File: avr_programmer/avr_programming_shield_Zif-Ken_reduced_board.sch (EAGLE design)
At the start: 17 parts

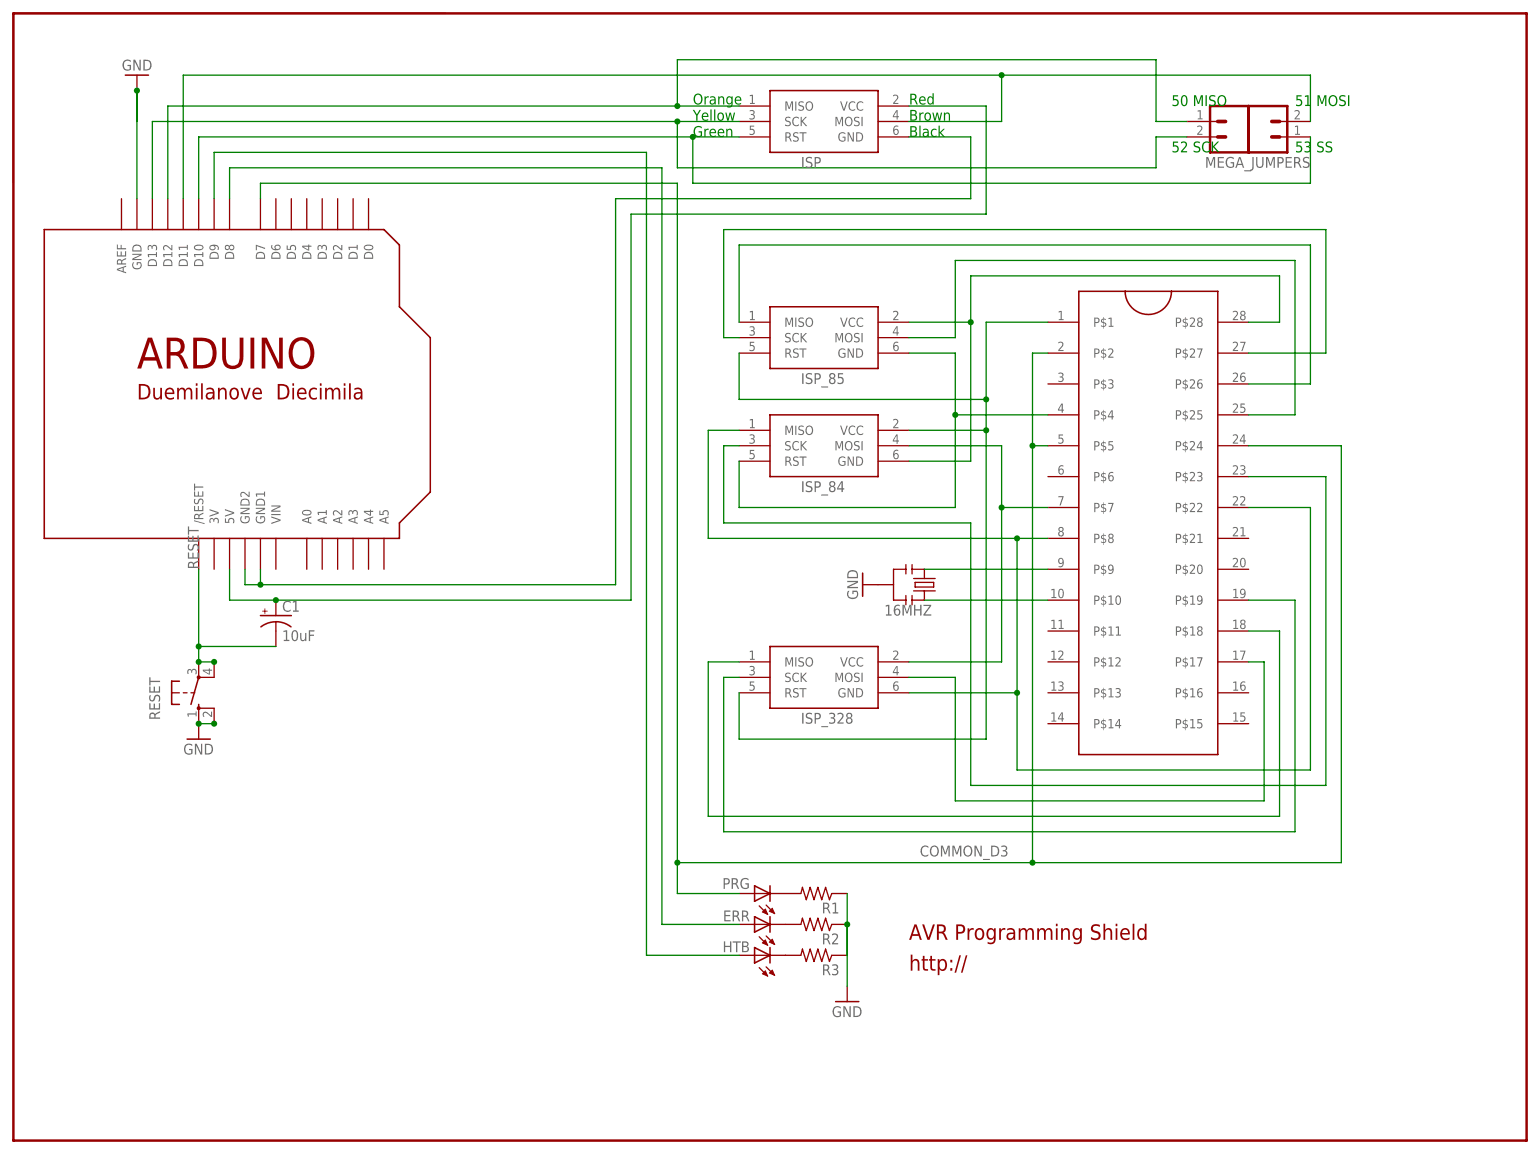
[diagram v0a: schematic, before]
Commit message: updating Zif footprint
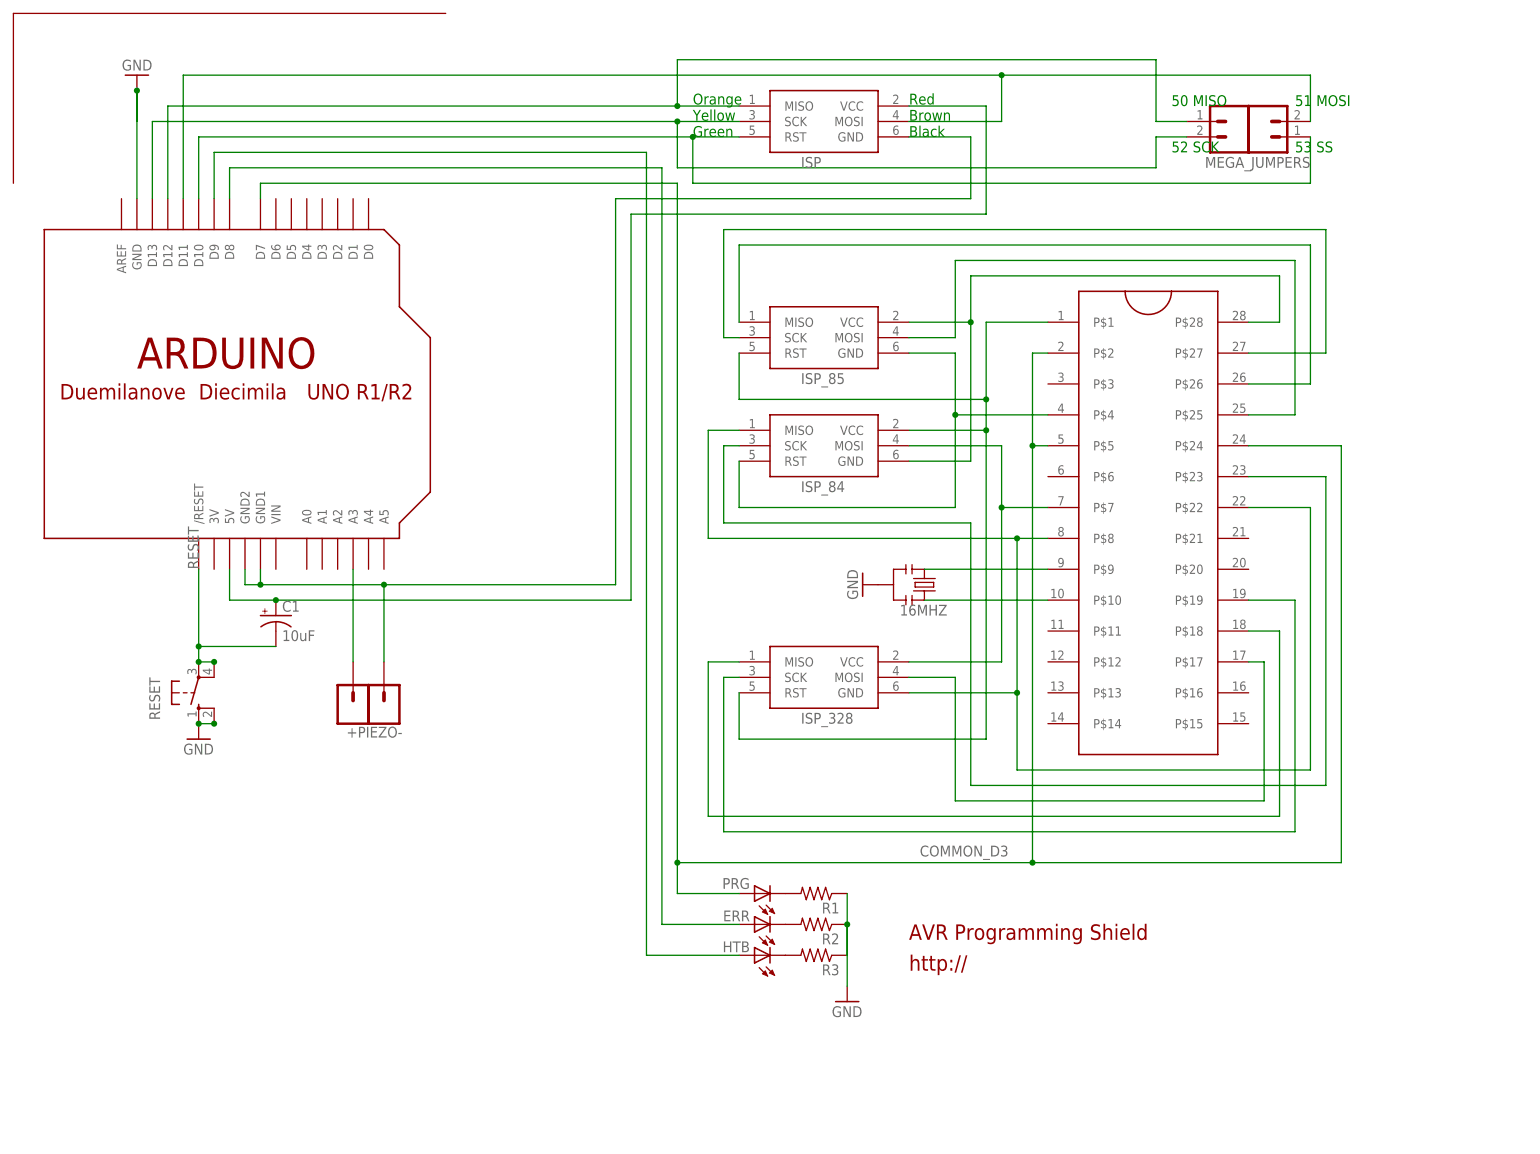
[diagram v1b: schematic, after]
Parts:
- removed U$3: ZIFSOCKET-28-3ZIFFSOCKET-28-3, SparkFun-Connectors_mod:ZIFSOCKET-28-3ZIFFSOCKET-28-3
- added +PIEZO-, JP4: M01PTH, SparkFun-Connectors_mod:M01PTH
- added U$4: ZIFSOCKET-28-3ZIFFSOCKET-28-3, SparkFun_mod:ZIFSOCKET-28-3ZIFFSOCKET-28-3
- 16MHZ: device SparkFun:RESONATORPTH -> SparkFun_mod:RESONATORPTH
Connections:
- new net N$12: JP4.1, U$1.A3
- net COMMON_D3: now also U$4.P$2, U$4.P$24, U$4.P$5; no longer U$3.P$2, U$3.P$24, U$3.P$5
- net GND: now also +PIEZO-.1
- net N$1: now also U$4.P$17; no longer U$3.P$17
- net N$11: now also U$4.P$7; no longer U$3.P$7
- net N$13: now also U$4.P$1; no longer U$3.P$1
- net N$15: now also U$4.P$23; no longer U$3.P$23
- net N$16: now also U$4.P$28; no longer U$3.P$28
- net N$18: now also U$4.P$4; no longer U$3.P$4
- net N$19: now also U$4.P$25; no longer U$3.P$25
- net N$20: now also U$4.P$26; no longer U$3.P$26
- net N$21: now also U$4.P$27; no longer U$3.P$27
- net N$22: now also U$4.P$9; no longer U$3.P$9
- net N$25: now also U$4.P$10; no longer U$3.P$10
- net N$26: now also U$4.P$22, U$4.P$8; no longer U$3.P$22, U$3.P$8
- net N$4: now also U$4.P$18; no longer U$3.P$18
- net N$7: now also U$4.P$19; no longer U$3.P$19
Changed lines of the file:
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@@
 <part name="ISP_85" library="adafruit" deviceset="AVRISP" device="-6"/>
 <part name="C1" library="SparkFun" deviceset="CAP_POL" device="PTH2" value="10uF"/>
-<part name="16MHZ" library="SparkFun" deviceset="RESONATOR" device="PTH"/>
 <part name="GND3" library="supply1" deviceset="GND" device=""/>
 <part name="MEGA_JUMPERS" library="SparkFun" deviceset="M02" device="PTH"/>
 <part name="JP2" library="SparkFun" deviceset="M02" device="PTH"/>
-<part name="U$3" library="SparkFun-Connectors_mod" deviceset="ZIFSOCKET-28-3" device="ZIFFSOCKET-28-3"/>
+<part name="16MHZ" library="SparkFun_mod" deviceset="RESONATOR" device="PTH"/>
+<part name="U$4" library="SparkFun_mod" deviceset="ZIFSOCKET-28-3" device="ZIFFSOCKET-28-3"/>
+<part name="JP4" library="SparkFun-Connectors_mod" deviceset="M01" device="PTH"/>
+<part name="+PIEZO-" library="SparkFun-Connectors_mod" deviceset="M01" device="PTH"/>
 </parts>
 <sheets>
@@
 <instance part="ISP_85" gate="G$1" x="132.08" y="132.08"/>
 <instance part="C1" gate="G$1" x="43.18" y="86.36"/>
-<instance part="16MHZ" gate="G$1" x="149.86" y="91.44" smashed="yes" rot="R270">
-<attribute name="NAME" x="143.256" y="86.36" size="1.778" layer="95"/>
-</instance>
 <instance part="GND3" gate="1" x="139.7" y="91.44" rot="R270"/>
 <instance part="MEGA_JUMPERS" gate="G$1" x="200.66" y="167.64" smashed="yes" rot="R180">
@@
 <attribute name="VALUE" x="203.2" y="160.02" size="1.778" layer="96"/>
 </instance>
-<instance part="U$3" gate="G$1" x="175.26" y="63.5"/>
+<instance part="16MHZ" gate="G$1" x="149.86" y="91.44" smashed="yes" rot="R270">
+<attribute name="NAME" x="145.796" y="86.36" size="1.778" layer="95"/>
+</instance>
+<instance part="U$4" gate="G$1" x="175.26" y="63.5"/>
+<instance part="JP4" gate="G$1" x="55.88" y="71.12" smashed="yes" rot="R90"/>
+<instance part="+PIEZO-" gate="G$1" x="60.96" y="71.12" smashed="yes" rot="R90">
+<attribute name="NAME" x="64.008" y="68.072" size="1.778" layer="95" rot="R180"/>
+</instance>
 </instances>
 <busses>
@@
 <wire x1="38.1" y1="93.98" x2="38.1" y2="91.44" width="0.1524" layer="91"/>
 <wire x1="38.1" y1="91.44" x2="40.64" y2="91.44" width="0.1524" layer="91"/>
-<wire x1="40.64" y1="91.44" x2="99.06" y2="91.44" width="0.1524" layer="91"/>
+<wire x1="40.64" y1="91.44" x2="60.96" y2="91.44" width="0.1524" layer="91"/>
+<wire x1="60.96" y1="91.44" x2="99.06" y2="91.44" width="0.1524" layer="91"/>
 <wire x1="99.06" y1="91.44" x2="99.06" y2="154.94" width="0.1524" layer="91"/>
 <wire x1="99.06" y1="154.94" x2="157.48" y2="154.94" width="0.1524" layer="91"/>
@@
 <pinref part="ISP" gate="G$1" pin="GND"/>
 <junction x="40.64" y="91.44"/>
+<wire x1="60.96" y1="78.74" x2="60.96" y2="91.44" width="0.1524" layer="91"/>
+<junction x="60.96" y="91.44"/>
+<pinref part="+PIEZO-" gate="G$1" pin="1"/>
 </segment>
 <segment>
@@
 <wire x1="205.74" y1="55.88" x2="205.74" y2="78.74" width="0.1524" layer="91"/>
 <wire x1="205.74" y1="78.74" x2="203.2" y2="78.74" width="0.1524" layer="91"/>
-<pinref part="U$3" gate="G$1" pin="P$17"/>
+<pinref part="U$4" gate="G$1" pin="P$17"/>
 </segment>
 </net>
@@
 <wire x1="208.28" y1="53.34" x2="208.28" y2="83.82" width="0.1524" layer="91"/>
 <wire x1="208.28" y1="83.82" x2="203.2" y2="83.82" width="0.1524" layer="91"/>
-<pinref part="U$3" gate="G$1" pin="P$18"/>
+<pinref part="U$4" gate="G$1" pin="P$18"/>
 </segment>
 </net>
@@
 <wire x1="210.82" y1="50.8" x2="210.82" y2="88.9" width="0.1524" layer="91"/>
 <wire x1="210.82" y1="88.9" x2="203.2" y2="88.9" width="0.1524" layer="91"/>
-<pinref part="U$3" gate="G$1" pin="P$19"/>
+<pinref part="U$4" gate="G$1" pin="P$19"/>
 </segment>
 </net>
@@
 <wire x1="162.56" y1="104.14" x2="170.18" y2="104.14" width="0.1524" layer="91"/>
 <junction x="162.56" y="104.14"/>
-<pinref part="U$3" gate="G$1" pin="P$7"/>
+<pinref part="U$4" gate="G$1" pin="P$7"/>
 </segment>
 </net>
@@
 <junction x="160.02" y="121.92"/>
 <pinref part="ISP_85" gate="G$1" pin="RST"/>
-<pinref part="U$3" gate="G$1" pin="P$1"/>
+<pinref part="U$4" gate="G$1" pin="P$1"/>
 </segment>
 </net>
@@
 <wire x1="215.9" y1="58.42" x2="215.9" y2="109.22" width="0.1524" layer="91"/>
 <wire x1="215.9" y1="109.22" x2="203.2" y2="109.22" width="0.1524" layer="91"/>
-<pinref part="U$3" gate="G$1" pin="P$23"/>
+<pinref part="U$4" gate="G$1" pin="P$23"/>
 </segment>
 </net>
@@
 <pinref part="ISP_85" gate="G$1" pin="VCC"/>
 <wire x1="147.32" y1="134.62" x2="157.48" y2="134.62" width="0.1524" layer="91"/>
-<pinref part="U$3" gate="G$1" pin="P$28"/>
+<pinref part="U$4" gate="G$1" pin="P$28"/>
 </segment>
 </net>
@@
 <wire x1="154.94" y1="129.54" x2="154.94" y2="119.38" width="0.1524" layer="91"/>
 <junction x="154.94" y="119.38"/>
-<pinref part="U$3" gate="G$1" pin="P$4"/>
+<pinref part="U$4" gate="G$1" pin="P$4"/>
 </segment>
 </net>
@@
 <wire x1="210.82" y1="144.78" x2="210.82" y2="119.38" width="0.1524" layer="91"/>
 <wire x1="210.82" y1="119.38" x2="203.2" y2="119.38" width="0.1524" layer="91"/>
-<pinref part="U$3" gate="G$1" pin="P$25"/>
+<pinref part="U$4" gate="G$1" pin="P$25"/>
 </segment>
 </net>
@@
 <wire x1="213.36" y1="147.32" x2="213.36" y2="124.46" width="0.1524" layer="91"/>
 <wire x1="213.36" y1="124.46" x2="203.2" y2="124.46" width="0.1524" layer="91"/>
-<pinref part="U$3" gate="G$1" pin="P$26"/>
+<pinref part="U$4" gate="G$1" pin="P$26"/>
 </segment>
 </net>
@@
 <wire x1="215.9" y1="149.86" x2="215.9" y2="129.54" width="0.1524" layer="91"/>
 <wire x1="215.9" y1="129.54" x2="203.2" y2="129.54" width="0.1524" layer="91"/>
-<pinref part="U$3" gate="G$1" pin="P$27"/>
+<pinref part="U$4" gate="G$1" pin="P$27"/>
 </segment>
 </net>
@@
 <wire x1="167.64" y1="45.72" x2="109.22" y2="45.72" width="0.1524" layer="91"/>
 <junction x="109.22" y="45.72"/>
-<pinref part="U$3" gate="G$1" pin="P$2"/>
-<pinref part="U$3" gate="G$1" pin="P$5"/>
-<pinref part="U$3" gate="G$1" pin="P$24"/>
+<pinref part="U$4" gate="G$1" pin="P$2"/>
+<pinref part="U$4" gate="G$1" pin="P$5"/>
+<pinref part="U$4" gate="G$1" pin="P$24"/>
 </segment>
 </net>
@@
 <net name="N$22" class="0">
 <segment>
+<wire x1="149.86" y1="93.98" x2="170.18" y2="93.98" width="0.1524" layer="91"/>
 <pinref part="16MHZ" gate="G$1" pin="1"/>
-<wire x1="149.86" y1="93.98" x2="170.18" y2="93.98" width="0.1524" layer="91"/>
-<pinref part="U$3" gate="G$1" pin="P$9"/>
+<pinref part="U$4" gate="G$1" pin="P$9"/>
 </segment>
 </net>
 <net name="N$25" class="0">
 <segment>
+<wire x1="149.86" y1="88.9" x2="170.18" y2="88.9" width="0.1524" layer="91"/>
 <pinref part="16MHZ" gate="G$1" pin="3"/>
-<wire x1="149.86" y1="88.9" x2="170.18" y2="88.9" width="0.1524" layer="91"/>
-<pinref part="U$3" gate="G$1" pin="P$10"/>
+<pinref part="U$4" gate="G$1" pin="P$10"/>
 </segment>
 </net>
@@
 <wire x1="114.3" y1="99.06" x2="165.1" y2="99.06" width="0.1524" layer="91"/>
 <junction x="165.1" y="99.06"/>
-<pinref part="U$3" gate="G$1" pin="P$8"/>
-<pinref part="U$3" gate="G$1" pin="P$22"/>
-</segment>
-</net>
+<pinref part="U$4" gate="G$1" pin="P$8"/>
+<pinref part="U$4" gate="G$1" pin="P$22"/>
+</segment>
+</net>
+<net name="N$12" class="0">
+<segment>
+<pinref part="U$1" gate="G$1" pin="A3"/>
+<wire x1="55.88" y1="78.74" x2="55.88" y2="93.98" width="0.1524" layer="91"/>
+<pinref part="JP4" gate="G$1" pin="1"/>
+</segment>
+</net>
